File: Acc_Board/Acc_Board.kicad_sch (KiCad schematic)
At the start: 39 parts, among them J1 1053091202, J3 1053091202, J4 1053091202, J5 1053091202, J6 1053091202, K1 Relay_SPST-NO, U1 ISO1050DUB, U13 R-78B5.0-2.0, U2 NUCLEO-L432KC, U4 PQDE6W-Q110-S5-H-D

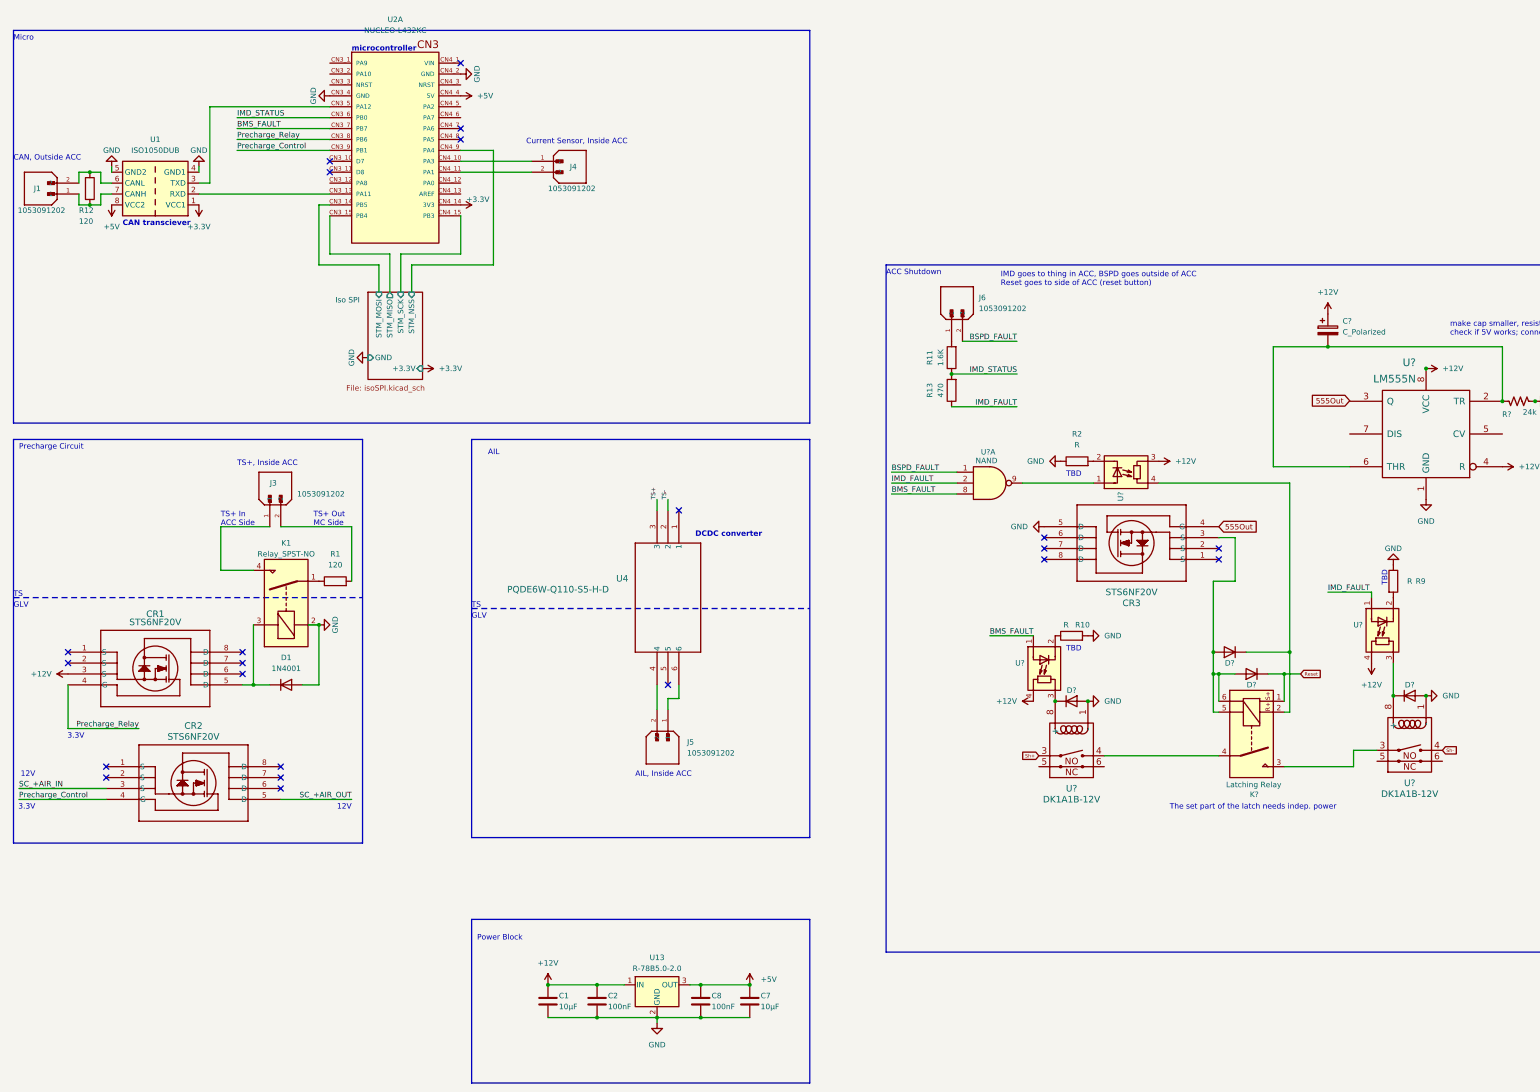
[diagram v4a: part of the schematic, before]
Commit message: Minor ACC board fixes
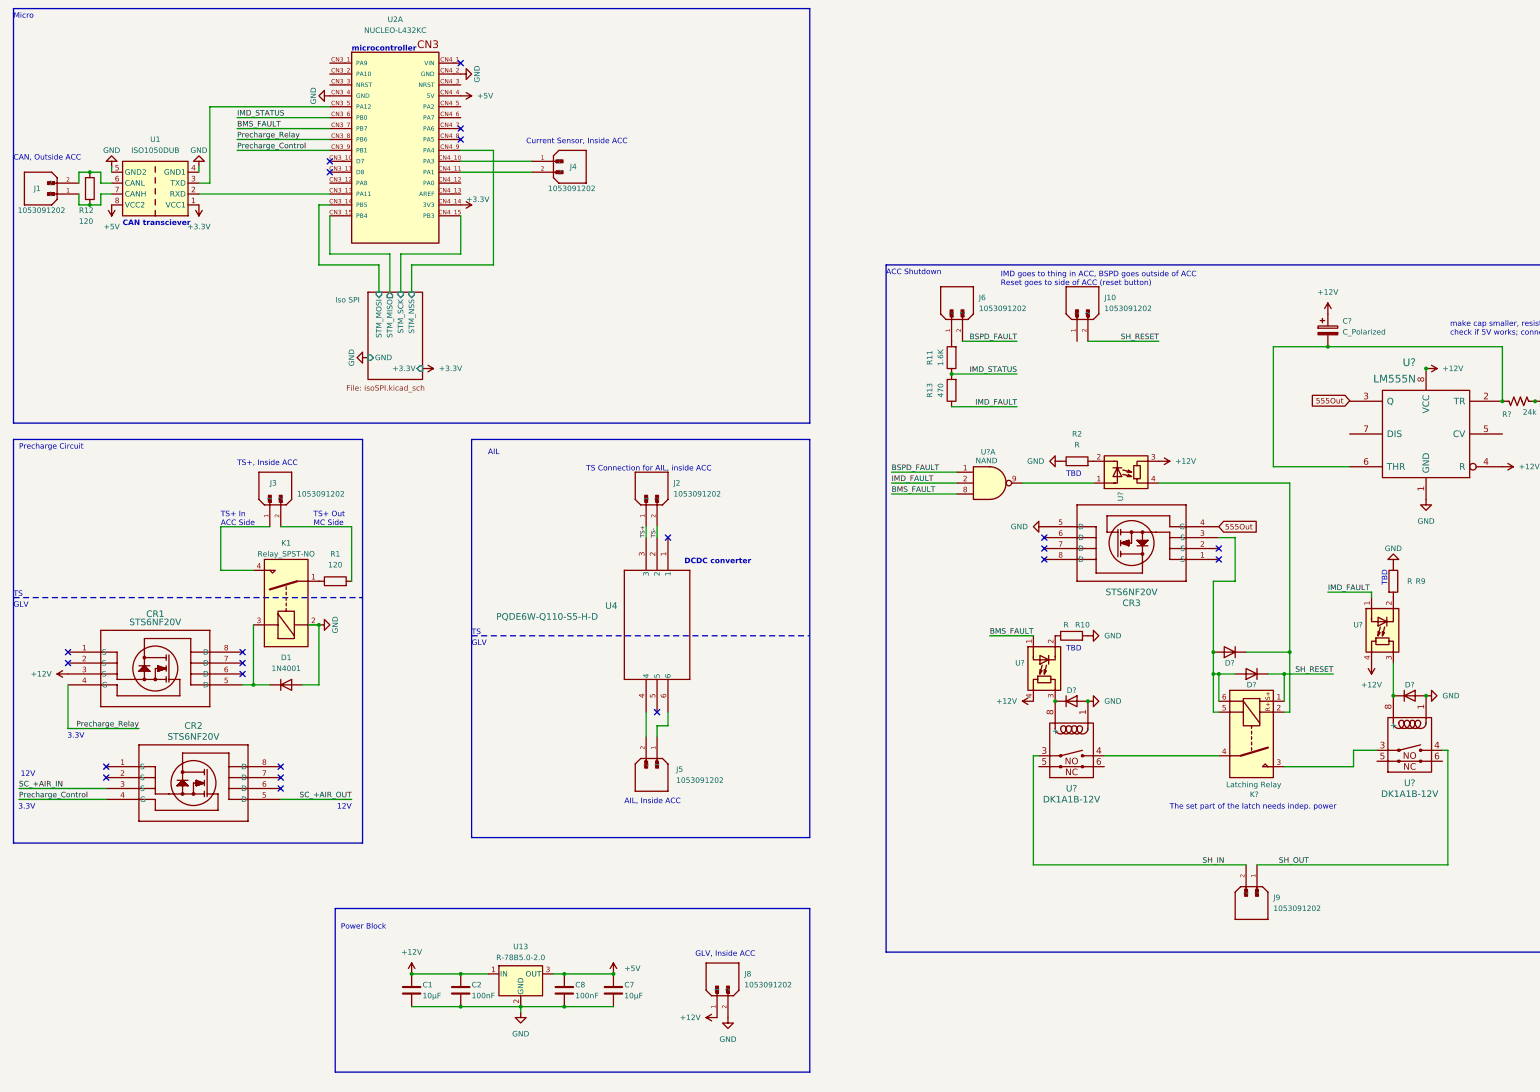
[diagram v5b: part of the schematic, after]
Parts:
- added J10, J2, J8, J9: 1053091202, 1FS_2_Global_Footprint_Library:MOLEX_1053091202, symbol molex_1053091202:1053091202
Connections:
- net +12V: now also J8.1
- net GND: now also J8.2
- net TS+: now also J2.1
- net TS-: now also J2.2
- net Reset renamed SH_RESET
- net SH_RESET: now also J10.2
- net Sh+ renamed SH_IN
- net SH_IN: now also J9.2
- net Sh- renamed SH_OUT
- net SH_OUT: now also J9.1
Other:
- note added: "GLV, Inside ACC"
- note added: "TS Connection for AIL, inside ACC"
- moved on the sheet: C1, C2, C7, C8, J5, U13, U4

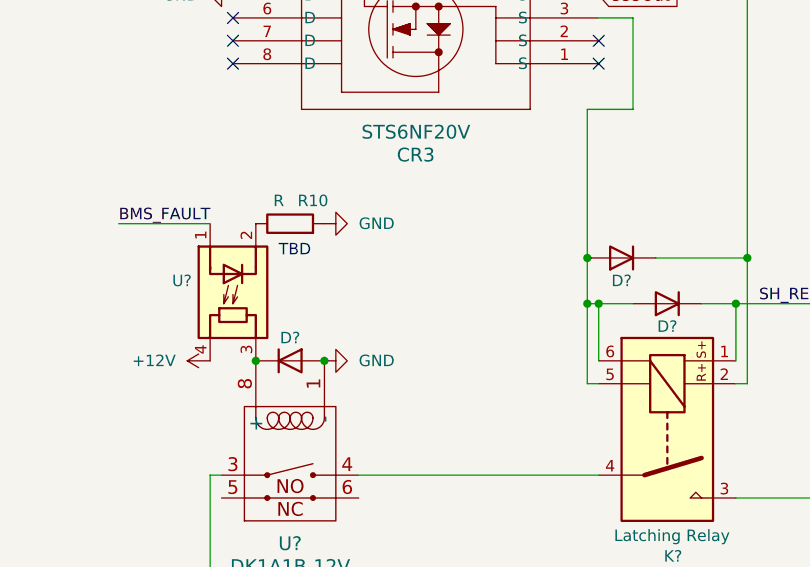
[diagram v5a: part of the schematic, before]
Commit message: small opto datasheet note
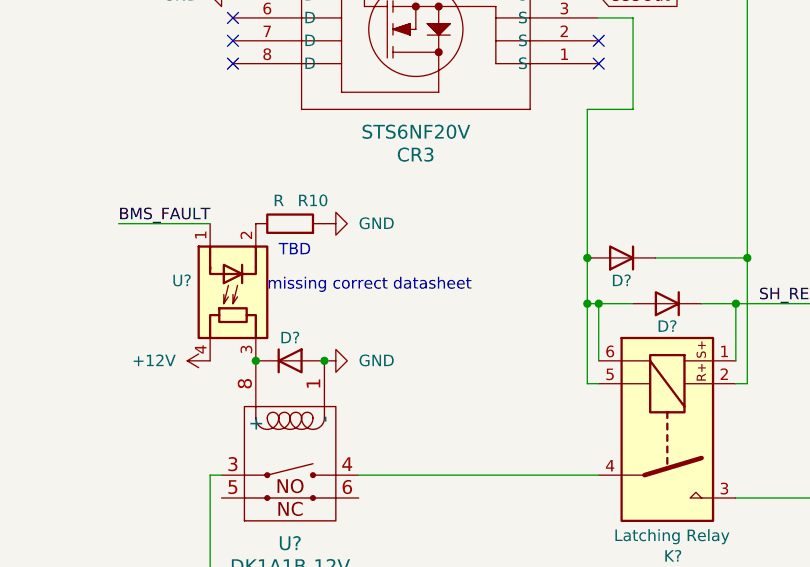
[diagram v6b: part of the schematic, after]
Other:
- note added: "missing correct datasheet"
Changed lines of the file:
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@@
+    (effects (font (size 1.27 1.27)) (justify left bottom))
+  )
+  (text "missing correct datasheet\n" (at 266.7 168.91 0)
     (effects (font (size 1.27 1.27)) (justify left bottom))
   )
@@
       (effects (font (size 1.27 1.27)) hide)
     )
-    (pin "2")
-    (pin "1")
+    (pin "1")
+    (pin "2")
     (instances
       (project "Acc_Board"
@@
       (effects (font (size 1.27 1.27)) hide)
     )
-    (pin "2")
-    (pin "1")
+    (pin "1")
+    (pin "2")
     (instances
       (project "Acc_Board"
@@
       (effects (font (size 1.27 1.27)) hide)
     )
+    (pin "1")
+    (pin "2")
     (pin "3")
-    (pin "2")
-    (pin "1")
-    (instances
-      (project "Acc_Board"
+    (instances
+      (project "Acc_Board"

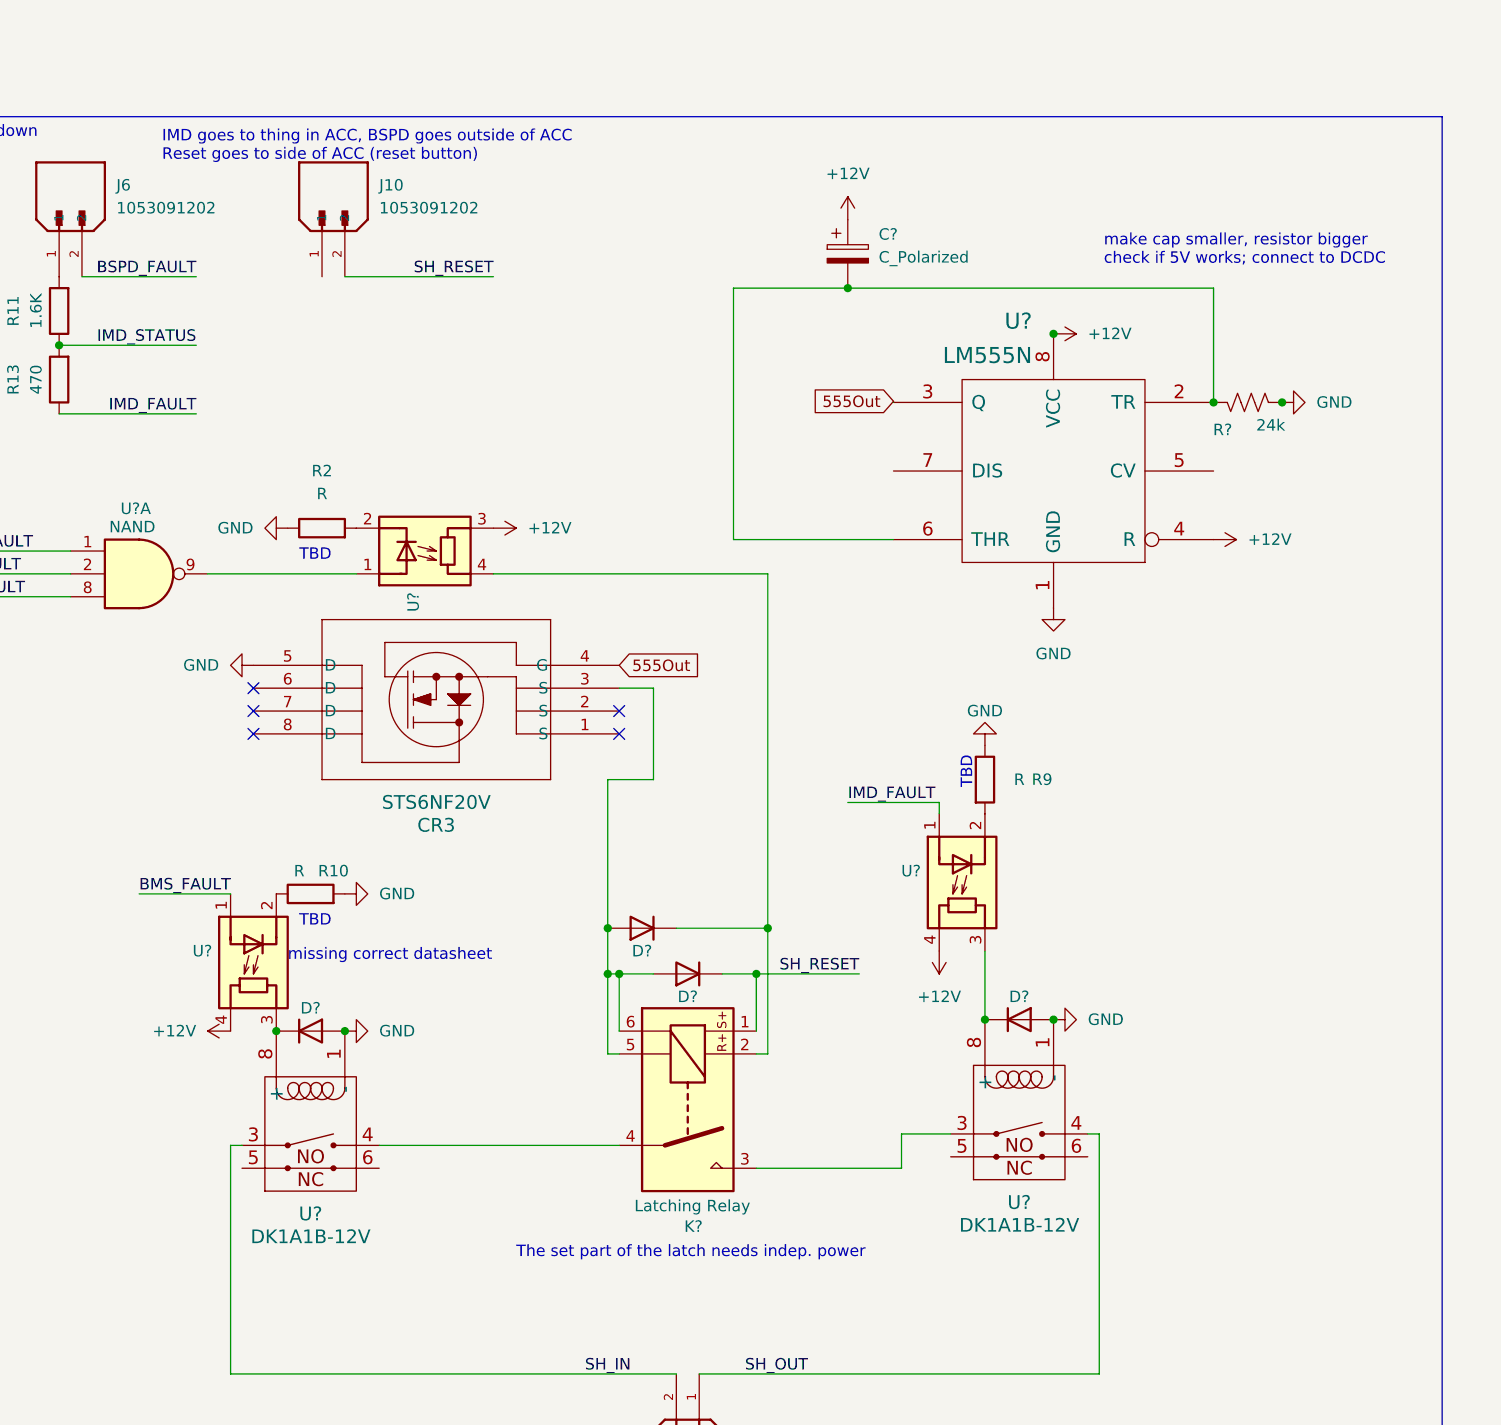
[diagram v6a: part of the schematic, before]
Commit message: +resistor to optos, +mosfet and timing to BSPD
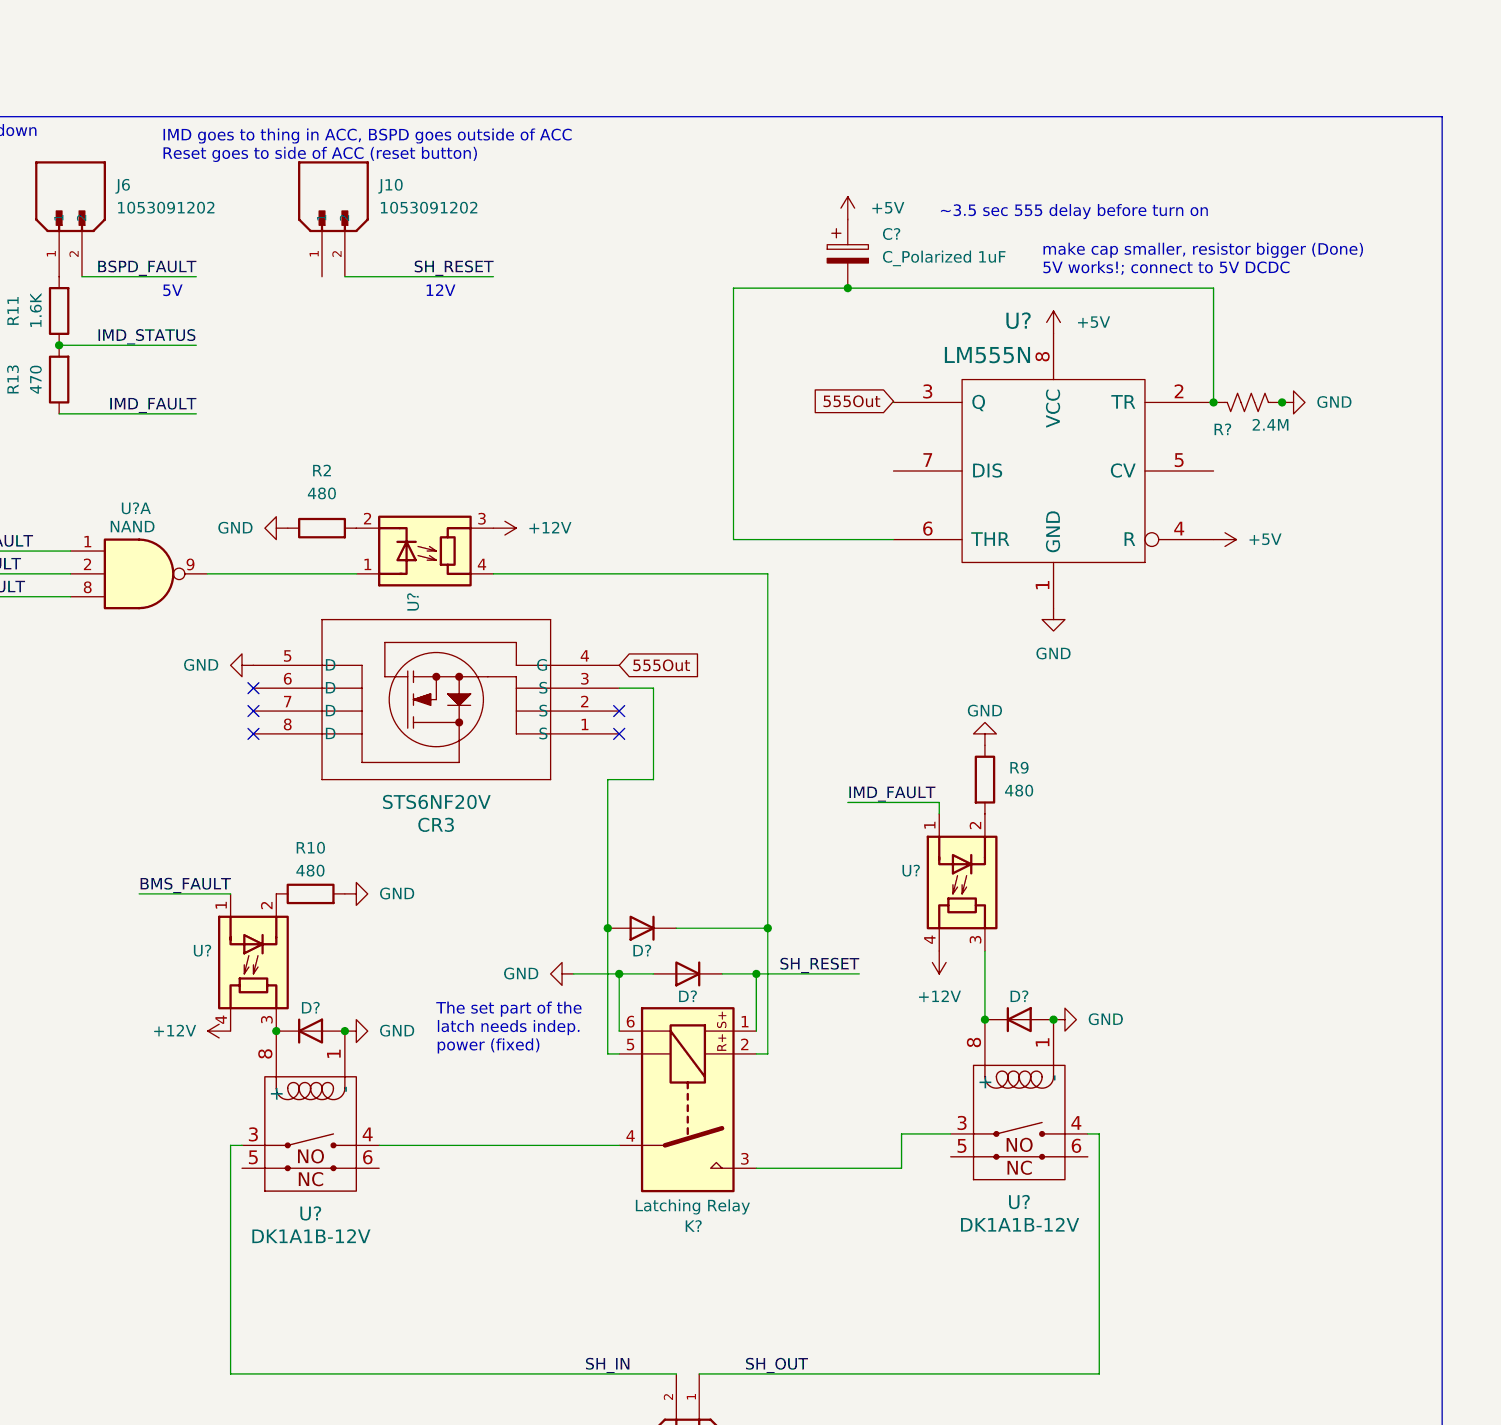
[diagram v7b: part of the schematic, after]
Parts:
- C?: value C_Polarized -> C_Polarized 1uF
- R10, R2, R9: value R -> 480
- R?: value 24k -> 2.4M
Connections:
- net +12V: no longer C?.1, U?.4 (R), U?.8 (VCC)
- net +5V: now also C?.1, U?.4 (R), U?.8 (VCC)
- net GND: now also D?.2 (A), K?.6
- net at CR3.3 (S), D?.2 (A), K?.5: no longer D?.2 (A), K?.6
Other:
- note added: "5V"
- note added: "The set part of the latch needs indep. power (fixed)"
- note added: "make cap smaller, resistor bigger (Done) 5V works!; connect to 5V DCDC"
- note added: "~3.5 sec 555 delay before turn on"
- note removed: "TBD"
- note removed: "The set part of the latch needs indep. power"
- note removed: "make cap smaller, resistor bigger check if 5V works; connect to DCDC"
- note removed: "missing correct datasheet"
